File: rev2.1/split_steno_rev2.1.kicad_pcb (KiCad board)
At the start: 2 copper layers, 99.4 x 76 mm, 76 parts, among them J1 USB_OTG, J2 Audio-Jack-4, P1 TC2030-IDC, SW1 SW_Push, SW10 SW_Push, SW11 SW_Push, SW12 SW_Push, SW13 SW_Push, SW14 SW_Push, SW15 SW_Push, SW16 SW_Push, SW17 SW_Push, SW18 SW_Push, SW19 SW_Push, SW2 SW_Push, SW20 SW_Push, SW21 SW_Push, SW22 Switch-6P-2S2T, SW3 SW_Push, SW4 SW_Push, SW5 SW_Push, SW6 SW_Push, SW7 SW_Push, SW8 SW_Push, SW9 SW_Push, U1 74LVC1G34, U2 MCP73831, U3 MCP1700, U4 MCP1700, U5 ATXMEGA128A4U-AU, U6 nRF24L01_module

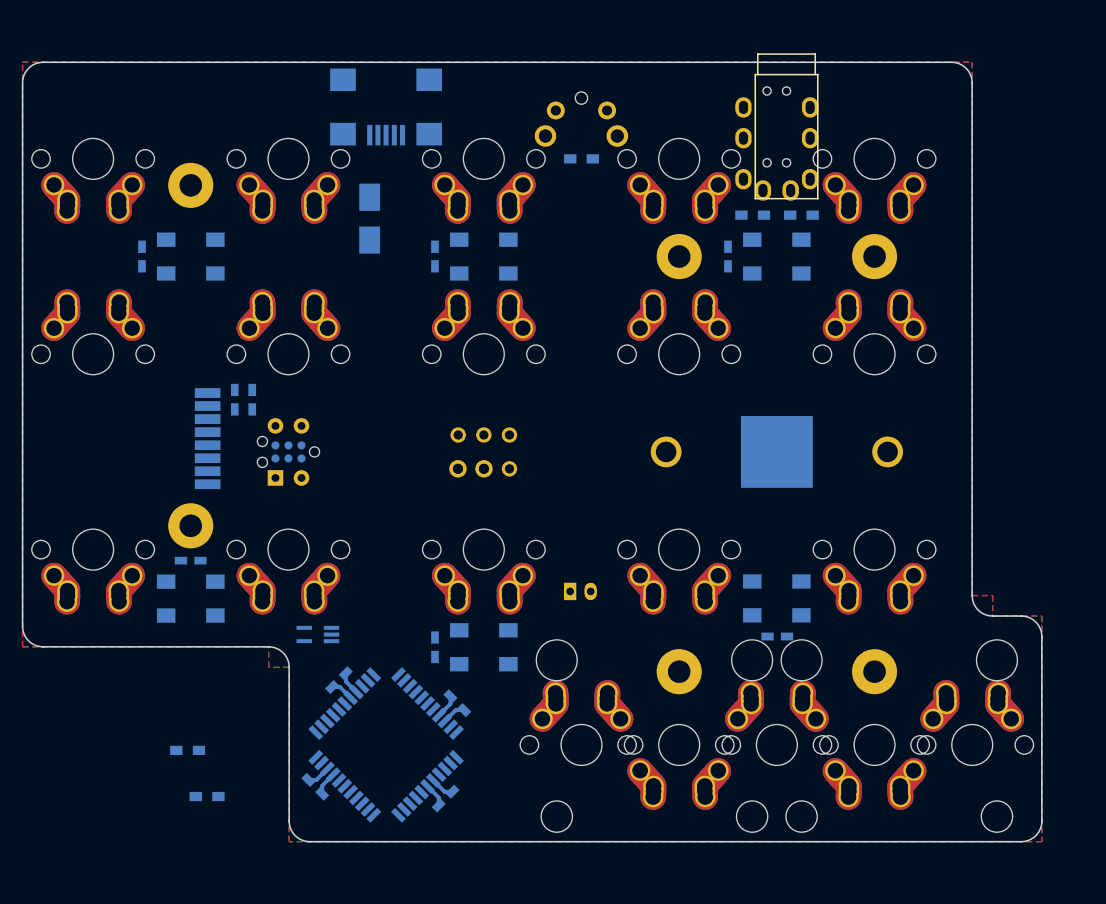
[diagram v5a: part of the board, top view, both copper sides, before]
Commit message: redid edge cuts tighter to switches
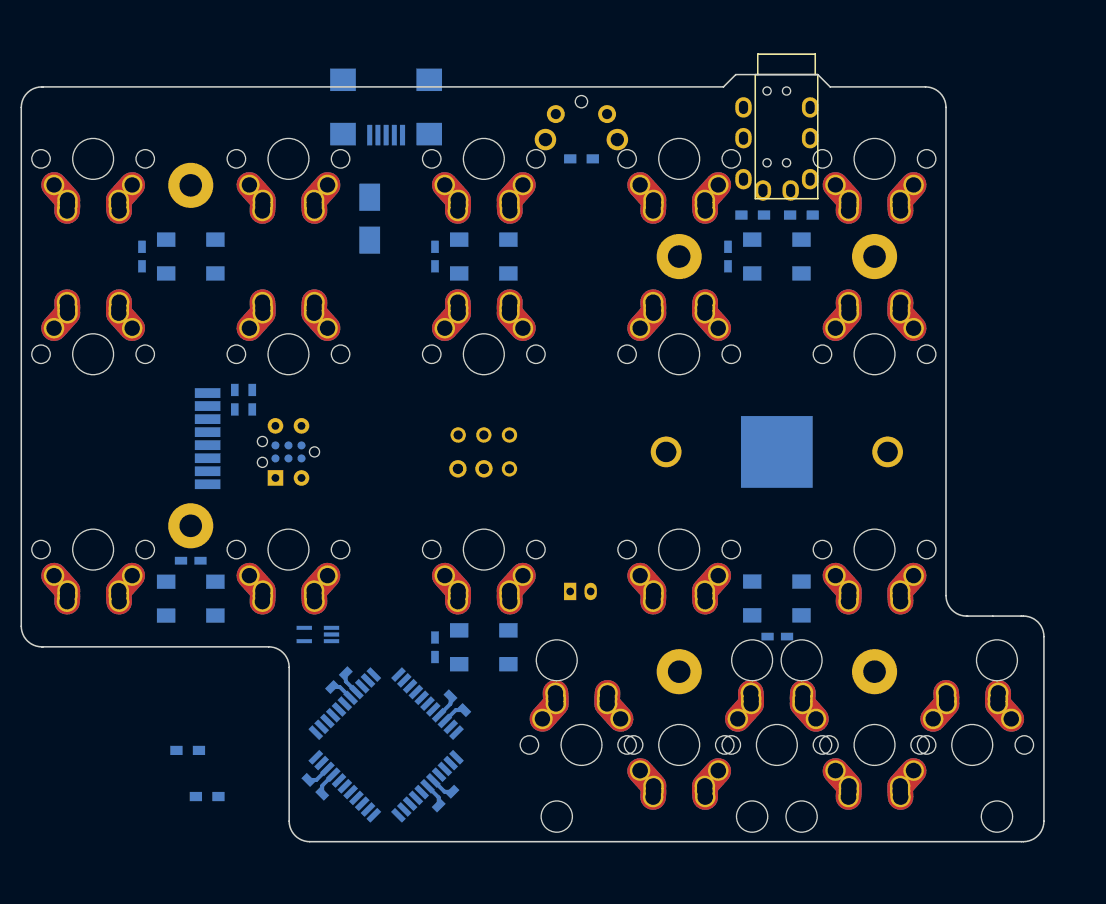
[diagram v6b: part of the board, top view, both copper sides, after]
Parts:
- moved SW21 0.35 mm to (90.6, 69.5)
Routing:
- removed copper zone on B.Cu, net GND
- removed copper zone on F.Cu, net GND
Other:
- board size 99.4 x 76 mm -> 99.7 x 74.8 mm
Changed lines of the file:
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@@
   (general
     (links 448)
-    (no_connects 134)
-    (area 33.524999 64.324999 133.075001 140.475001)
+    (no_connects 158)
+    (area 33.399999 65.524999 133.275001 140.475001)
     (thickness 1.6)
-    (drawings 16)
+    (drawings 26)
     (tracks 16)
     (zones 0)
@@
     (41 Cmts.User user)
     (42 Eco1.User user)
-    (43 Eco2.User user)
+    (43 Eco2.User user hide)
     (44 Edge.Cuts user)
     (45 Margin user)
-    (46 B.CrtYd user)
+    (46 B.CrtYd user hide)
     (47 F.CrtYd user)
     (48 B.Fab user)
@@
   )
   (module Keebio-Parts:SW_Tactile_SPST_Angled_MJTP1117 (layer B.Cu)
-    (at 90.6 69.1 180)
+    (at 90.6 69.45 180)
     (descr "tactile switch SPST right angle, PTS645VL39-2 LFS")
     (tags "tactile switch SPST angled PTS645VL39-2 LFS C&K Button")
@@
     )
   )
-  (gr_line (start 35.6 64.4) (end 124.2 64.4) (angle 90) (layer Edge.Cuts) (width 0.15))
-  (gr_line (start 126.2 116.4) (end 126.2 66.4) (angle 90) (layer Edge.Cuts) (width 0.15))
+  (gr_line (start 101.95 66.8) (end 35.6 66.8) (angle 90) (layer Edge.Cuts) (width 0.15))
+  (gr_line (start 103.15 65.6) (end 101.95 66.8) (angle 90) (layer Edge.Cuts) (width 0.15))
+  (gr_line (start 112.35 66.8) (end 121.65 66.8) (angle 90) (layer Edge.Cuts) (width 0.15))
+  (gr_line (start 111.15 65.6) (end 112.35 66.8) (angle 90) (layer Edge.Cuts) (width 0.15))
+  (gr_line (start 103.15 65.6) (end 111.15 65.6) (angle 90) (layer Edge.Cuts) (width 0.15))
+  (gr_line (start 123.65 116.4) (end 123.65 68.8) (angle 90) (layer Edge.Cuts) (width 0.15))
+  (gr_line (start 125.75 118.4) (end 128.2 118.4) (angle 90) (layer Edge.Cuts) (width 0.15))
+  (gr_line (start 33.475 68.8) (end 33.475 119.4) (angle 90) (layer Edge.Cuts) (width 0.15))
+  (gr_line (start 125.65 118.4) (end 125.75 118.4) (angle 90) (layer Edge.Cuts) (width 0.15))
+  (gr_line (start 133.2 138.4) (end 133.2 120.4) (angle 90) (layer Edge.Cuts) (width 0.15))
+  (gr_line (start 59.6 123.4) (end 59.6 138.4) (angle 90) (layer Edge.Cuts) (width 0.15))
+  (gr_line (start 35.6 121.4) (end 35.475 121.4) (angle 90) (layer Edge.Cuts) (width 0.15))
+  (gr_line (start 35.475 66.8) (end 35.6 66.8) (angle 90) (layer Edge.Cuts) (width 0.15))
+  (gr_line (start 131 118.4) (end 131.2 118.4) (angle 90) (layer Edge.Cuts) (width 0.15))
+  (gr_line (start 131 140.4) (end 131.2 140.4) (angle 90) (layer Edge.Cuts) (width 0.15))
   (gr_line (start 128.2 118.4) (end 131 118.4) (angle 90) (layer Edge.Cuts) (width 0.15))
-  (gr_arc (start 128.2 116.4) (end 128.2 118.4) (angle 90) (layer Edge.Cuts) (width 0.15))
-  (gr_line (start 133 138.4) (end 133 120.4) (angle 90) (layer Edge.Cuts) (width 0.15))
-  (gr_line (start 33.6 119.4) (end 33.6 66.4) (angle 90) (layer Edge.Cuts) (width 0.15))
+  (gr_arc (start 125.65 116.4) (end 125.65 118.4) (angle 90) (layer Edge.Cuts) (width 0.15))
   (gr_line (start 57.6 121.4) (end 35.6 121.4) (angle 90) (layer Edge.Cuts) (width 0.15))
-  (gr_line (start 59.6 123.4) (end 59.6 138.4) (angle 90) (layer Edge.Cuts) (width 0.15))
   (gr_line (start 61.6 140.4) (end 131 140.4) (angle 90) (layer Edge.Cuts) (width 0.15))
-  (gr_arc (start 131 120.4) (end 131 118.4) (angle 90) (layer Edge.Cuts) (width 0.15))
-  (gr_arc (start 35.6 66.4) (end 33.6 66.4) (angle 90) (layer Edge.Cuts) (width 0.15))
-  (gr_arc (start 35.6 119.4) (end 35.6 121.4) (angle 90) (layer Edge.Cuts) (width 0.15))
-  (gr_arc (start 124.2 66.4) (end 124.2 64.4) (angle 90) (layer Edge.Cuts) (width 0.15))
+  (gr_arc (start 131.2 120.4) (end 131.2 118.4) (angle 90) (layer Edge.Cuts) (width 0.15))
+  (gr_arc (start 35.475 68.8) (end 33.475 68.8) (angle 90) (layer Edge.Cuts) (width 0.15))
+  (gr_arc (start 35.475 119.4) (end 35.475 121.4) (angle 90) (layer Edge.Cuts) (width 0.15))
+  (gr_arc (start 121.65 68.8) (end 121.65 66.8) (angle 90) (layer Edge.Cuts) (width 0.15))
   (gr_arc (start 57.6 123.4) (end 57.6 121.4) (angle 90) (layer Edge.Cuts) (width 0.15))
   (gr_arc (start 61.6 138.4) (end 61.6 140.4) (angle 90) (layer Edge.Cuts) (width 0.15))
-  (gr_arc (start 131 138.4) (end 133 138.4) (angle 90) (layer Edge.Cuts) (width 0.15))
+  (gr_arc (start 131.2 138.4) (end 133.2 138.4) (angle 90) (layer Edge.Cuts) (width 0.15))
   (segment (start 63.778249 125.321751) (end 64.540622 125.321751) (width 0.381) (layer B.Cu) (net 2))
   (segment (start 64.540622 125.321751) (end 65.591427 126.372556) (width 0.381) (layer B.Cu) (net 2))
@@
   (segment (start 74.178249 136.871751) (end 74.178249 136.090749) (width 0.381) (layer B.Cu) (net 6))
   (segment (start 74.178249 136.090749) (end 73.086759 134.999259) (width 0.381) (layer B.Cu) (net 6))
-  (zone (net 2) (net_name GND) (layer F.Cu) (hatch edge 0.508)
-    (connect_pads (clearance 0.508))
-    (min_thickness 0.254)
-    (fill yes (arc_segments 16) (thermal_gap 0.508) (thermal_bridge_width 0.508))
-    (polygon
-      (pts
-        (xy 126.2 116.4) (xy 128.2 116.4) (xy 128.2 118.4) (xy 133 118.4) (xy 133 140.4)
-        (xy 59.6 140.4) (xy 59.6 123.4) (xy 57.6 123.4) (xy 57.6 121.4) (xy 33.6 121.4)
-        (xy 33.6 64.4) (xy 126.2 64.4)
-      )
-    )
-  )
-  (zone (net 2) (net_name GND) (layer B.Cu) (hatch edge 0.508)
-    (connect_pads (clearance 0.508))
-    (min_thickness 0.254)
-    (fill yes (arc_segments 16) (thermal_gap 0.508) (thermal_bridge_width 0.508))
-    (polygon
-      (pts
-        (xy 126.2 116.4) (xy 128.2 116.4) (xy 128.2 118.4) (xy 133 118.4) (xy 133 140.4)
-        (xy 59.6 140.4) (xy 59.6 123.4) (xy 57.6 123.4) (xy 57.6 121.4) (xy 33.6 121.4)
-        (xy 33.6 64.4) (xy 126.2 64.4)
-      )
-    )
-  )
 )

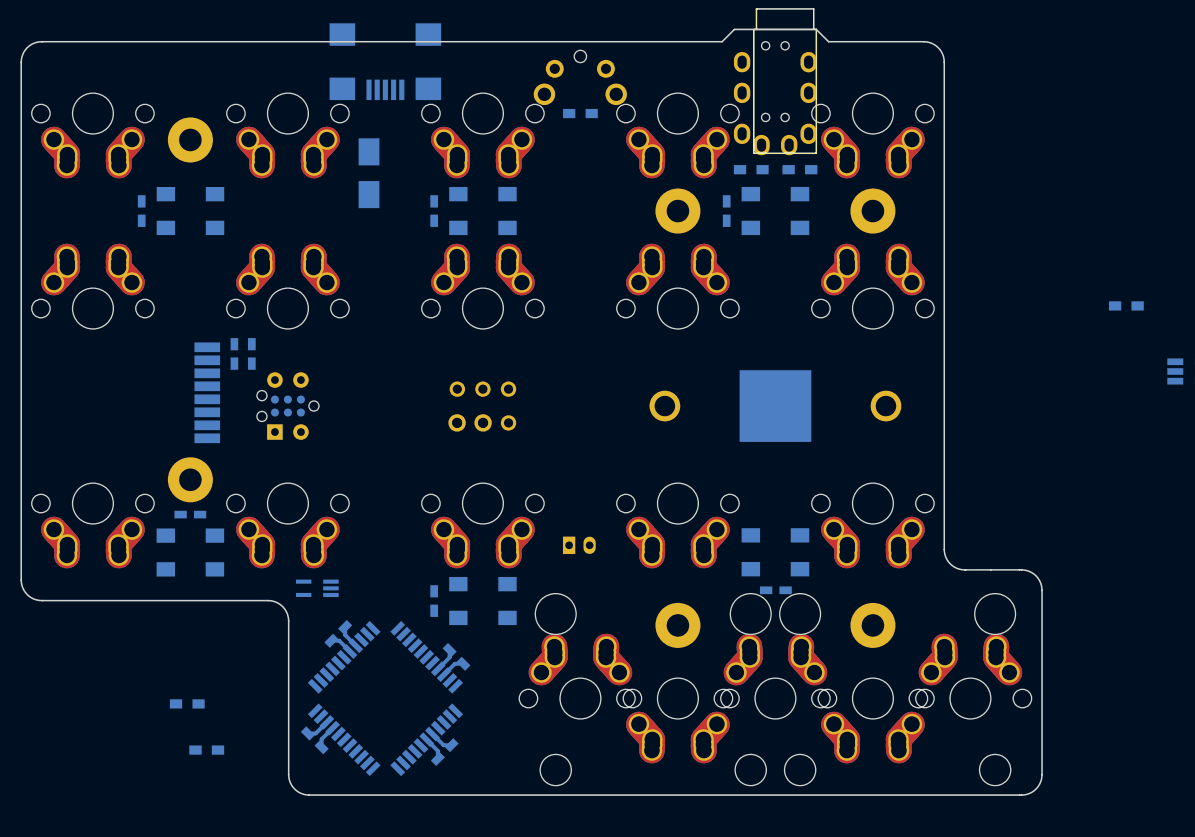
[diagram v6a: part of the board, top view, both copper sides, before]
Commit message: begin working on plate design (cherry+alps with cherry stabilizers)
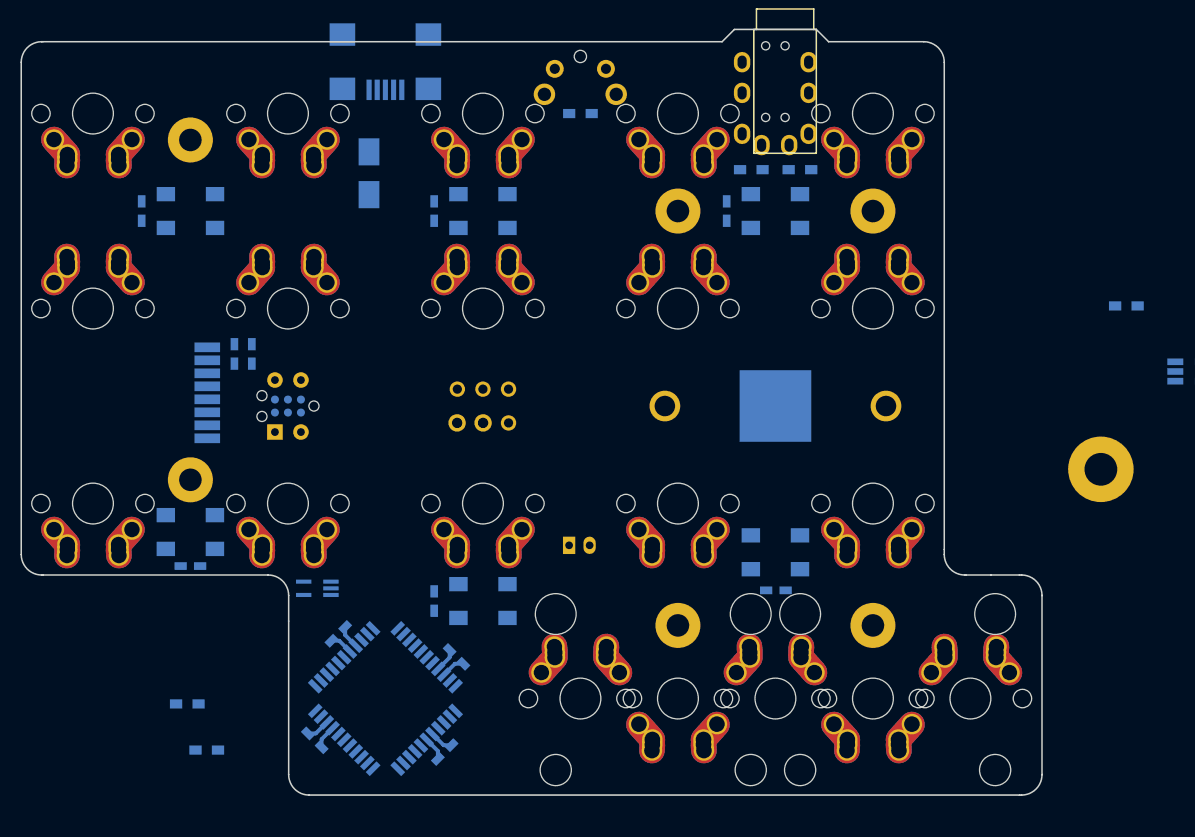
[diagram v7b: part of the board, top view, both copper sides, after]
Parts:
- added ?: , Mounting_Holes:MountingHole_3.2mm_M3_Pad, F.Cu at (138.9, 108.6)
- moved C1 5.03 mm to (50.0, 118.0)
- moved LED1 2.00 mm to (50.0, 114.7)
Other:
- outline, holes or cut-outs redrawn
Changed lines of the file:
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@@
     (area 33.399999 65.524999 133.275001 140.475001)
     (thickness 1.6)
-    (drawings 26)
+    (drawings 28)
     (tracks 16)
     (zones 0)
-    (modules 76)
+    (modules 77)
     (nets 60)
   )
@@
   )
   (module Capacitors_SMD:C_0603_HandSoldering (layer B.Cu)
-    (at 50 113)
+    (at 50 118.025)
     (descr "Capacitor SMD 0603, hand soldering")
     (tags "capacitor 0603")
@@
   )
   (module WS2812B:WS2812B (layer B.Cu)
-    (at 50 116.7 270)
+    (at 50 114.7 270)
     (fp_text reference LED1 (at 0 4.7 270) (layer B.SilkS)
       (effects (font (size 1 1) (thickness 0.2)) (justify mirror))
@@
     )
   )
+  (module Mounting_Holes:MountingHole_3.2mm_M3_Pad (layer F.Cu)
+    (at 138.95 108.575)
+    (descr "Mounting Hole 3.2mm, M3")
+    (tags "mounting hole 3.2mm m3")
+    (fp_text reference "" (at 0 -4.2) (layer F.SilkS)
+      (effects (font (size 1 1) (thickness 0.15)))
+    )
+    (fp_text value "" (at 0 4.2) (layer F.Fab)
+      (effects (font (size 1 1) (thickness 0.15)))
+    )
+    (fp_circle (center 0 0) (end 3.2 0) (layer Cmts.User) (width 0.15))
+    (fp_circle (center 0 0) (end 3.45 0) (layer F.CrtYd) (width 0.05))
+    (pad 1 thru_hole circle (at 0 0) (size 6.4 6.4) (drill 3.2) (layers *.Cu *.Mask))
+  )
+  (gr_line (start 33.475 116.9) (end 33.475 68.8) (angle 90) (layer Edge.Cuts) (width 0.15))
+  (gr_line (start 59.6 123.4) (end 59.6 120.9) (angle 90) (layer Edge.Cuts) (width 0.15))
+  (gr_line (start 123.65 116.9) (end 123.65 116.4) (angle 90) (layer Edge.Cuts) (width 0.15))
+  (gr_line (start 133.2 138.4) (end 133.2 120.9) (angle 90) (layer Edge.Cuts) (width 0.15))
   (gr_line (start 101.95 66.8) (end 35.6 66.8) (angle 90) (layer Edge.Cuts) (width 0.15))
   (gr_line (start 103.15 65.6) (end 101.95 66.8) (angle 90) (layer Edge.Cuts) (width 0.15))
@@
   (gr_line (start 103.15 65.6) (end 111.15 65.6) (angle 90) (layer Edge.Cuts) (width 0.15))
   (gr_line (start 123.65 116.4) (end 123.65 68.8) (angle 90) (layer Edge.Cuts) (width 0.15))
-  (gr_line (start 125.75 118.4) (end 128.2 118.4) (angle 90) (layer Edge.Cuts) (width 0.15))
-  (gr_line (start 33.475 68.8) (end 33.475 119.4) (angle 90) (layer Edge.Cuts) (width 0.15))
-  (gr_line (start 125.65 118.4) (end 125.75 118.4) (angle 90) (layer Edge.Cuts) (width 0.15))
-  (gr_line (start 133.2 138.4) (end 133.2 120.4) (angle 90) (layer Edge.Cuts) (width 0.15))
+  (gr_line (start 125.75 118.9) (end 128.2 118.9) (angle 90) (layer Edge.Cuts) (width 0.15))
+  (gr_line (start 125.65 118.9) (end 125.75 118.9) (angle 90) (layer Edge.Cuts) (width 0.15))
   (gr_line (start 59.6 123.4) (end 59.6 138.4) (angle 90) (layer Edge.Cuts) (width 0.15))
-  (gr_line (start 35.6 121.4) (end 35.475 121.4) (angle 90) (layer Edge.Cuts) (width 0.15))
+  (gr_line (start 35.6 118.9) (end 35.475 118.9) (angle 90) (layer Edge.Cuts) (width 0.15))
   (gr_line (start 35.475 66.8) (end 35.6 66.8) (angle 90) (layer Edge.Cuts) (width 0.15))
-  (gr_line (start 131 118.4) (end 131.2 118.4) (angle 90) (layer Edge.Cuts) (width 0.15))
+  (gr_line (start 131 118.9) (end 131.2 118.9) (angle 90) (layer Edge.Cuts) (width 0.15))
   (gr_line (start 131 140.4) (end 131.2 140.4) (angle 90) (layer Edge.Cuts) (width 0.15))
-  (gr_line (start 128.2 118.4) (end 131 118.4) (angle 90) (layer Edge.Cuts) (width 0.15))
-  (gr_arc (start 125.65 116.4) (end 125.65 118.4) (angle 90) (layer Edge.Cuts) (width 0.15))
-  (gr_line (start 57.6 121.4) (end 35.6 121.4) (angle 90) (layer Edge.Cuts) (width 0.15))
+  (gr_line (start 128.2 118.9) (end 131 118.9) (angle 90) (layer Edge.Cuts) (width 0.15))
+  (gr_arc (start 125.65 116.9) (end 125.65 118.9) (angle 90) (layer Edge.Cuts) (width 0.15))
+  (gr_line (start 57.6 118.9) (end 35.6 118.9) (angle 90) (layer Edge.Cuts) (width 0.15))
   (gr_line (start 61.6 140.4) (end 131 140.4) (angle 90) (layer Edge.Cuts) (width 0.15))
-  (gr_arc (start 131.2 120.4) (end 131.2 118.4) (angle 90) (layer Edge.Cuts) (width 0.15))
+  (gr_arc (start 131.2 120.9) (end 131.2 118.9) (angle 90) (layer Edge.Cuts) (width 0.15))
   (gr_arc (start 35.475 68.8) (end 33.475 68.8) (angle 90) (layer Edge.Cuts) (width 0.15))
-  (gr_arc (start 35.475 119.4) (end 35.475 121.4) (angle 90) (layer Edge.Cuts) (width 0.15))
+  (gr_arc (start 35.475 116.9) (end 35.475 118.9) (angle 90) (layer Edge.Cuts) (width 0.15))
   (gr_arc (start 121.65 68.8) (end 121.65 66.8) (angle 90) (layer Edge.Cuts) (width 0.15))
-  (gr_arc (start 57.6 123.4) (end 57.6 121.4) (angle 90) (layer Edge.Cuts) (width 0.15))
+  (gr_arc (start 57.6 120.9) (end 57.6 118.9) (angle 90) (layer Edge.Cuts) (width 0.15))
   (gr_arc (start 61.6 138.4) (end 61.6 140.4) (angle 90) (layer Edge.Cuts) (width 0.15))
   (gr_arc (start 131.2 138.4) (end 133.2 138.4) (angle 90) (layer Edge.Cuts) (width 0.15))

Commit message: removed lipo charging circuit
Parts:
- removed the ? at (138.9, 108.6)
- removed BT2: Battery_Cell, Connectors_JST:JST_PH_S2B-PH-K_02x2.00mm_Angled
- removed C15, C16: 4.7uF, Capacitors_SMD:C_0603_HandSoldering
- removed C7: 1uF, Capacitors_SMD:C_0603_HandSoldering
- removed R1: 10k, Resistors_SMD:R_0603_HandSoldering
- removed R2, R3: 470k, Resistors_SMD:R_0603_HandSoldering
- removed U2: MCP73831, TO_SOT_Packages_SMD:SOT-23-5_HandSoldering
- removed U3: MCP1700, TO_SOT_Packages_SMD:SOT-23
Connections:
- net /BAT_IN renamed Net-(BT1-Pad1)
- U5 pad 12: /BAT_PROG -> Net-(U5-Pad12)
- U5 pad 13: /BAT_STAT -> Net-(U5-Pad13)
